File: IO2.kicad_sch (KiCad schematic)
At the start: 35 parts, among them J901 Conn_01x03_Pin, J902 Conn_01x03_Pin, J903 Conn_01x03_Pin, J904 Conn_01x03_Pin, J905 Conn_01x03_Pin, J906 Conn_01x03_Pin, J907 Conn_01x03_Pin, J908 Conn_01x03_Pin, J909 Conn_01x03_Pin, J910 Conn_01x03_Pin, J911 Conn_01x03_Pin, J912 Conn_01x03_Pin, J913 12402012E212A, J914 SM04B-GHS-TB(LF)(SN), U901 USBLC6-2P6

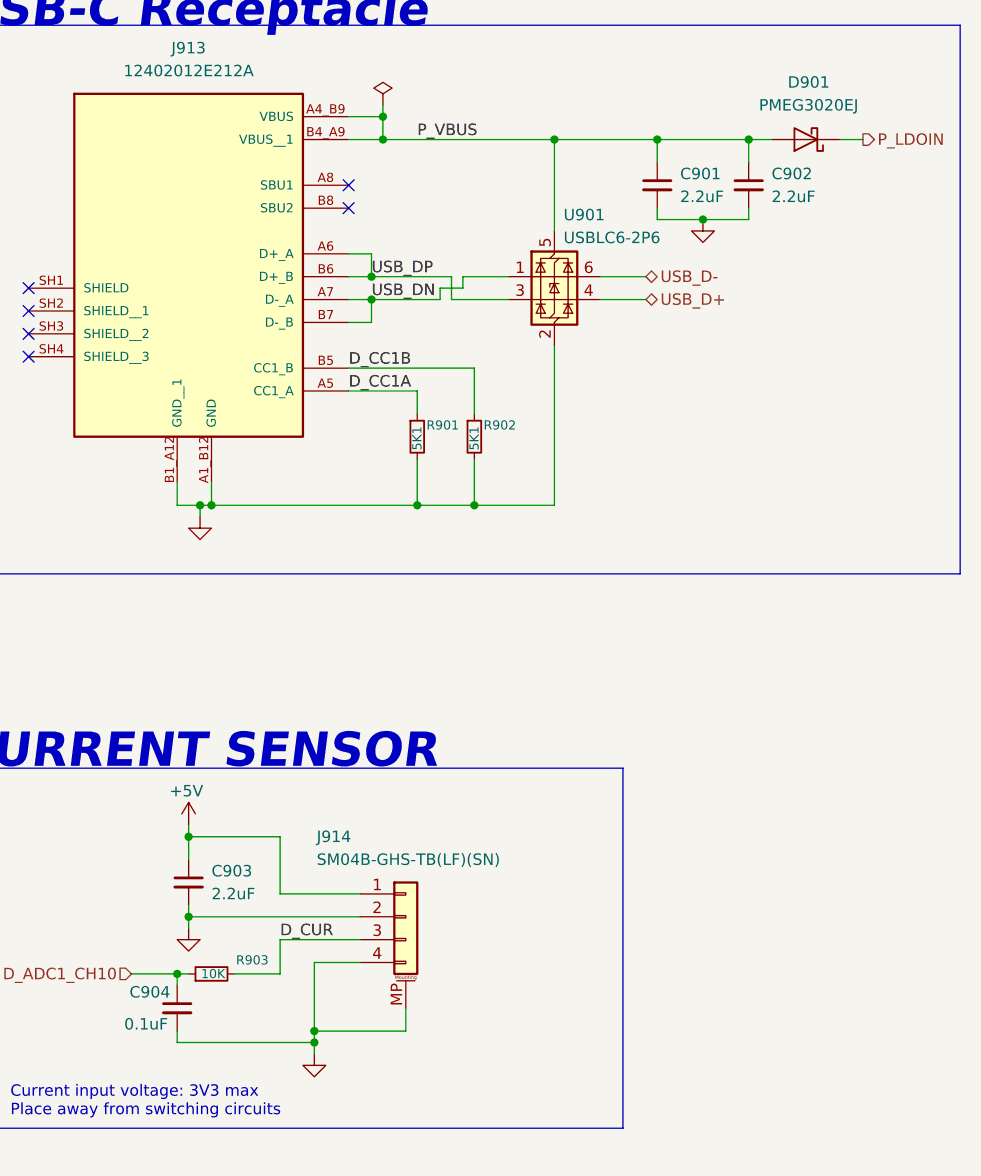
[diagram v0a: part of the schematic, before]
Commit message: refactor: change tim5 ch 1 label to ch 2
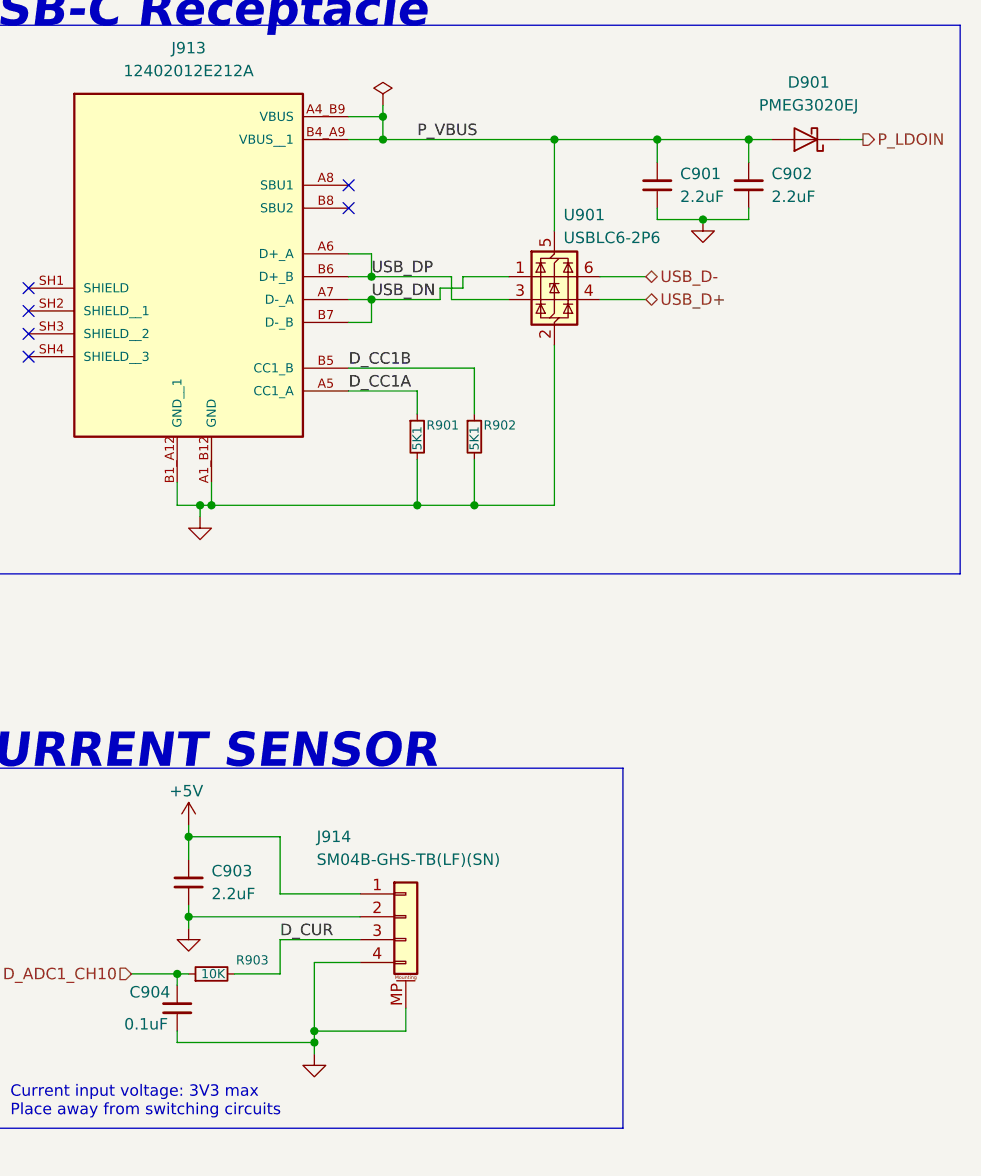
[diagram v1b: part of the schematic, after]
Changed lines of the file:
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@@
 		(fields_autoplaced yes)
 		(property "Reference" "C902"
-			(at 256.54 48.2662 0)
+			(at 256.54 48.2599 0)
 			(show_name no)
 			(do_not_autoplace no)
@@
 		)
 		(property "Value" "2.2uF"
-			(at 256.54 50.8062 0)
+			(at 256.54 50.7999 0)
 			(show_name no)
 			(do_not_autoplace no)
@@
 			)
 		)
-		(property "Description" "Ceramic Capacitor, Ceramic, 16V, 20% +Tol, 20% -Tol, X7R, 15% TC, 2.2uF, Surface Mount, 0805"
-			(at 254 49.53 0)
+		(property "Description" "Unpolarized capacitor, small symbol"
+			(at 254 59.69 0)
 			(hide yes)
 			(show_name no)
@@
 		(fields_autoplaced yes)
 		(property "Reference" "C901"
-			(at 246.38 48.2662 0)
+			(at 246.38 48.2599 0)
 			(show_name no)
 			(do_not_autoplace no)
@@
 		)
 		(property "Value" "2.2uF"
-			(at 246.38 50.8062 0)
+			(at 246.38 50.7999 0)
 			(show_name no)
 			(do_not_autoplace no)
@@
 			)
 		)
-		(property "Description" "Ceramic Capacitor, Ceramic, 16V, 20% +Tol, 20% -Tol, X7R, 15% TC, 2.2uF, Surface Mount, 0805"
-			(at 243.84 49.53 0)
+		(property "Description" "Unpolarized capacitor, small symbol"
+			(at 243.84 59.69 0)
 			(hide yes)
 			(show_name no)
@@
 		)
 		(property "Description" "Unpolarized capacitor, small symbol"
-			(at 190.5 140.97 0)
+			(at 190.5 151.13 0)
 			(hide yes)
 			(show_name no)
@@
 		(fields_autoplaced yes)
 		(property "Reference" "C903"
-			(at 194.31 125.7362 0)
+			(at 194.31 125.7299 0)
 			(show_name no)
 			(do_not_autoplace no)
@@
 		)
 		(property "Value" "2.2uF"
-			(at 194.31 128.2762 0)
+			(at 194.31 128.2699 0)
 			(show_name no)
 			(do_not_autoplace no)
@@
 			)
 		)
-		(property "Description" "Ceramic Capacitor, Ceramic, 16V, 20% +Tol, 20% -Tol, X7R, 15% TC, 2.2uF, Surface Mount, 0805"
-			(at 191.77 127 0)
+		(property "Description" "Unpolarized capacitor, small symbol"
+			(at 191.77 137.16 0)
 			(hide yes)
 			(show_name no)

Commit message: fix!: change ouput 3 timer from tim4 ch4 to tim1 ch3
tim4 ch4 does not have dma. Therefore replaced it with tim1 ch3.
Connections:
- net D_TIM4_CH4 renamed D_TIM1_CH3
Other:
- note added: "(9) IO2"
- note added: "Current input voltage: 3V3 max Cut off freq: 159 Hz Place away from switching circuits"
- note removed: "Current input voltage: 3V3 max Place away from switching circuits"
- moved on the sheet: J901, J902, J903, J904, J905, J906, J907, J908, J909, J910, J911, J912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
